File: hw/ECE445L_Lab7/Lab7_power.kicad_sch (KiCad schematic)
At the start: 0 parts

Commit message: Created spice models for analog circuits, started kicad schematic -> right audio channel, screen, basic power
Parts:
- added C11, C12: 4.7u, ECE445L:C_Axial_200mil, symbol ECE445L:C
- added C13: 0.1u, ECE445L:C_Axial_200mil, symbol ECE445L:C
- added IC1: LP2950-33LPRE3, ECE445L:TL431CLPM, symbol ECE445L:LP2950-33LPRE3
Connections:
- new net +3V3: C12.1, C13.1, IC1.1 (OUTPUT)
- new net +VBat: C11.1, IC1.3 (INPUT)
- new net GND: C11.2, C12.2, C13.2, IC1.2 (GND)
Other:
- note added: "+3V3 Regulator"

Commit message: Updated hardware schematic
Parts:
- added IC3: LM4041CILPR, ECE445L:ti_LM4041CILPR, symbol ti_LM4041CILPR:LM4041CILPR
- added R3: 1k, symbol Device:R
- added R4: 47k, symbol Device:R
- added R5: 10k, symbol Device:R
- renumbered IC1 to U2
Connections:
- net +3V3: now also R3.1
- net GND: now also IC3.3, R5.2
- new net: IC3.2, R3.2, R4.1
- new net VRef: IC3.1, R4.2, R5.1
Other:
- note added: "Vref"

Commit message: More Updates to hardware
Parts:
- added J3: Barrel_Jack, symbol Connector:Barrel_Jack
- renumbered U2 to U4, IC3 to U7
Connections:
- net +VBat: now also J3.1
- net GND: now also J3.2
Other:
- note added: "Wallwort Connector"
- moved on the sheet: R3, R4, R5, U7

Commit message: Lab7A Schematic and BOM - Ashton
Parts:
- removed U4: LP2950-33LPRE3, ECE445L:TL431CLPM, symbol ECE445L:LP2950-33LPRE3
- added SW8: SW_SPST, symbol Switch:SW_SPST
- added TP1: +VRail, ECE445L:Testpoint_1x02_P2.54mm, symbol ECE445L:Testpoint
- added TP13: +VRef, ECE445L:Testpoint_1x02_P2.54mm, symbol ECE445L:Testpoint
- added TP2: 3V3, ECE445L:Testpoint_1x02_P2.54mm, symbol ECE445L:Testpoint
- added U4: LM2937ET-3.3_NOPB, ECE445L:TO254P470X1028X1955-3P, symbol ECE445L:LM2937ET-3.3_NOPB
- C12: renamed from C11; footprint ECE445L:C_Axial_200mil -> Capacitor_SMD:C_0805_2012Metric
- C13: renamed from C12; footprint ECE445L:C_Axial_200mil -> Capacitor_SMD:C_0805_2012Metric
- C14: renamed from C13; footprint ECE445L:C_Axial_200mil -> Capacitor_SMD:C_0603_1608Metric
- renumbered R3 to R60, R4 to R61, R5 to R62
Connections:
- net +3V3: now also TP2.1 (A), TP2.2 (B), U4.3 (OUTPUT)
- net GND: now also U4.2 (GND)
- net VRef: now also TP13.1 (A), TP13.2 (B)
- net +VBat: no longer names the net of J3.1
- net +VBat: now also SW8.1 (A); no longer C12.1
- new net +VRail: C12.1, SW8.2 (B), TP1.1 (A), TP1.2 (B), U4.1 (INPUT)

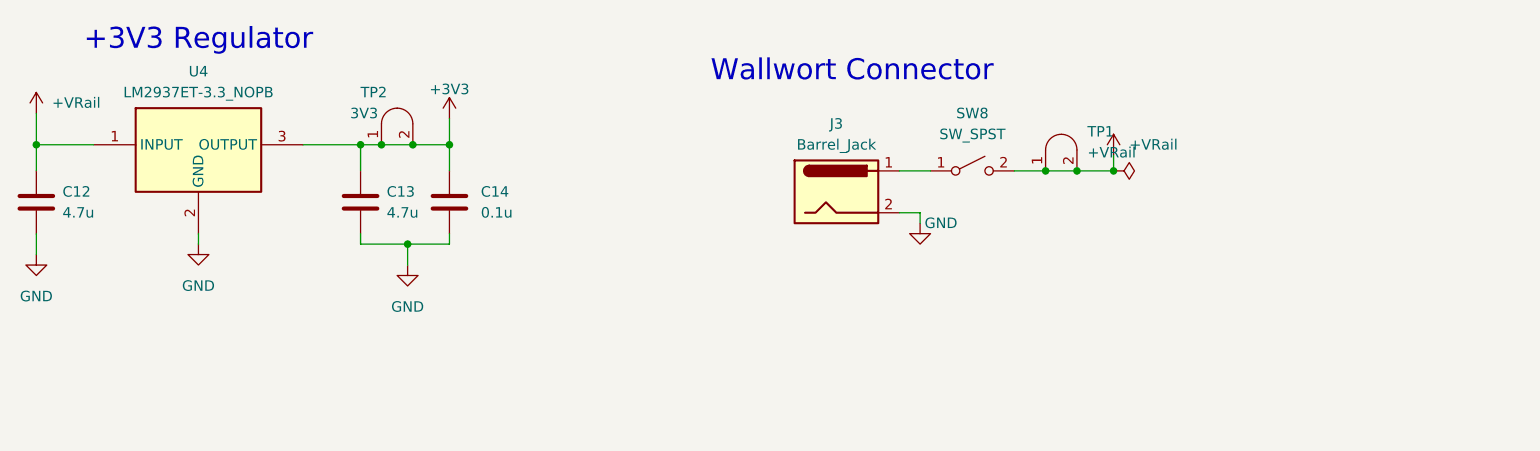
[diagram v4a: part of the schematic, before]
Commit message: Made changers to the schematic, updated bom, and created priliminary layout for the PCB. Ready for 7B Prep!
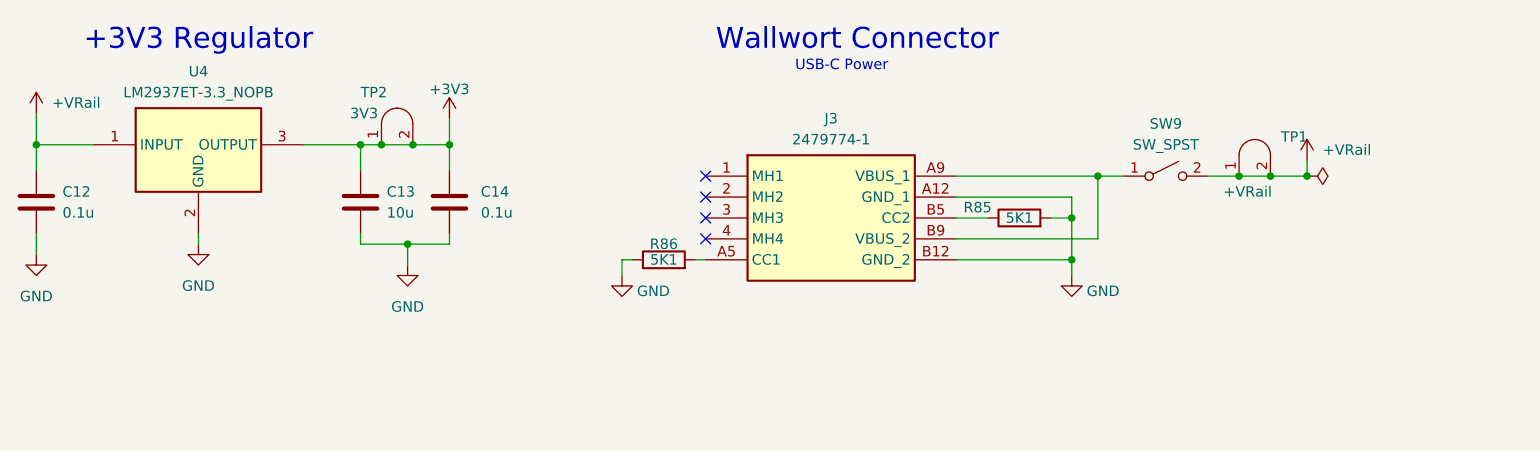
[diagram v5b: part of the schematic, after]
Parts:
- removed J3: Barrel_Jack, symbol Connector:Barrel_Jack
- added J3: 2479774-1, ECE445L:24797741, symbol 2479774-1:2479774-1
- added R85, R86: 5K1, Resistor_SMD:R_0603_1608Metric, symbol Device:R
- C12: value 4.7u -> 0.1u; footprint Capacitor_SMD:C_0805_2012Metric -> Capacitor_SMD:C_0603_1608Metric
- C13: value 4.7u -> 10u
- R60, R61, R62: footprint (none) -> Resistor_SMD:R_0603_1608Metric
- SW9: renamed from SW8; footprint (none) -> ECE445L:SW-T3-1A-A-A3-S1
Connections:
- net GND: now also J3.A12 (GND_1), J3.B12 (GND_2), R85.2, R86.1
- net at SW9.1 (A): now also J3.A9 (VBUS_1), J3.B9 (VBUS_2)
- new net: J3.B5 (CC2), R85.1
- new net: J3.A5 (CC1), R86.2
- no-connect marks 0 -> 4
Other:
- note added: "USB-C Power"
- moved on the sheet: SW9, TP1

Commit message: Rough draft layout - need to remove tm4c chip
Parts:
- C1: renamed from C12; footprint Capacitor_SMD:C_0603_1608Metric -> Capacitor_SMD:C_0603_1608Metric_Pad1.08x0.95mm_HandSolder
- C2: renamed from C13; footprint Capacitor_SMD:C_0805_2012Metric -> Capacitor_SMD:C_0805_2012Metric_Pad1.18x1.45mm_HandSolder
- C3: renamed from C14; footprint Capacitor_SMD:C_0603_1608Metric -> Capacitor_SMD:C_0603_1608Metric_Pad1.08x0.95mm_HandSolder
- R1: renamed from R86; footprint Resistor_SMD:R_0603_1608Metric -> Resistor_SMD:R_0603_1608Metric_Pad0.98x0.95mm_HandSolder
- R2: renamed from R85; footprint Resistor_SMD:R_0603_1608Metric -> Resistor_SMD:R_0603_1608Metric_Pad0.98x0.95mm_HandSolder
- R3: renamed from R60; footprint Resistor_SMD:R_0603_1608Metric -> Resistor_SMD:R_0603_1608Metric_Pad0.98x0.95mm_HandSolder
- R4: renamed from R61; footprint Resistor_SMD:R_0603_1608Metric -> Resistor_SMD:R_0603_1608Metric_Pad0.98x0.95mm_HandSolder
- R5: renamed from R62; footprint Resistor_SMD:R_0603_1608Metric -> Resistor_SMD:R_0603_1608Metric_Pad0.98x0.95mm_HandSolder
- renumbered J3 to J1, SW9 to SW1, TP2 to TP1, TP1 to TP2, TP13 to TP3, U4 to U1, U7 to U2
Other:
- company: (none) -> The University of Texas at Austin
- title: (none) -> ECE 445L Lab7

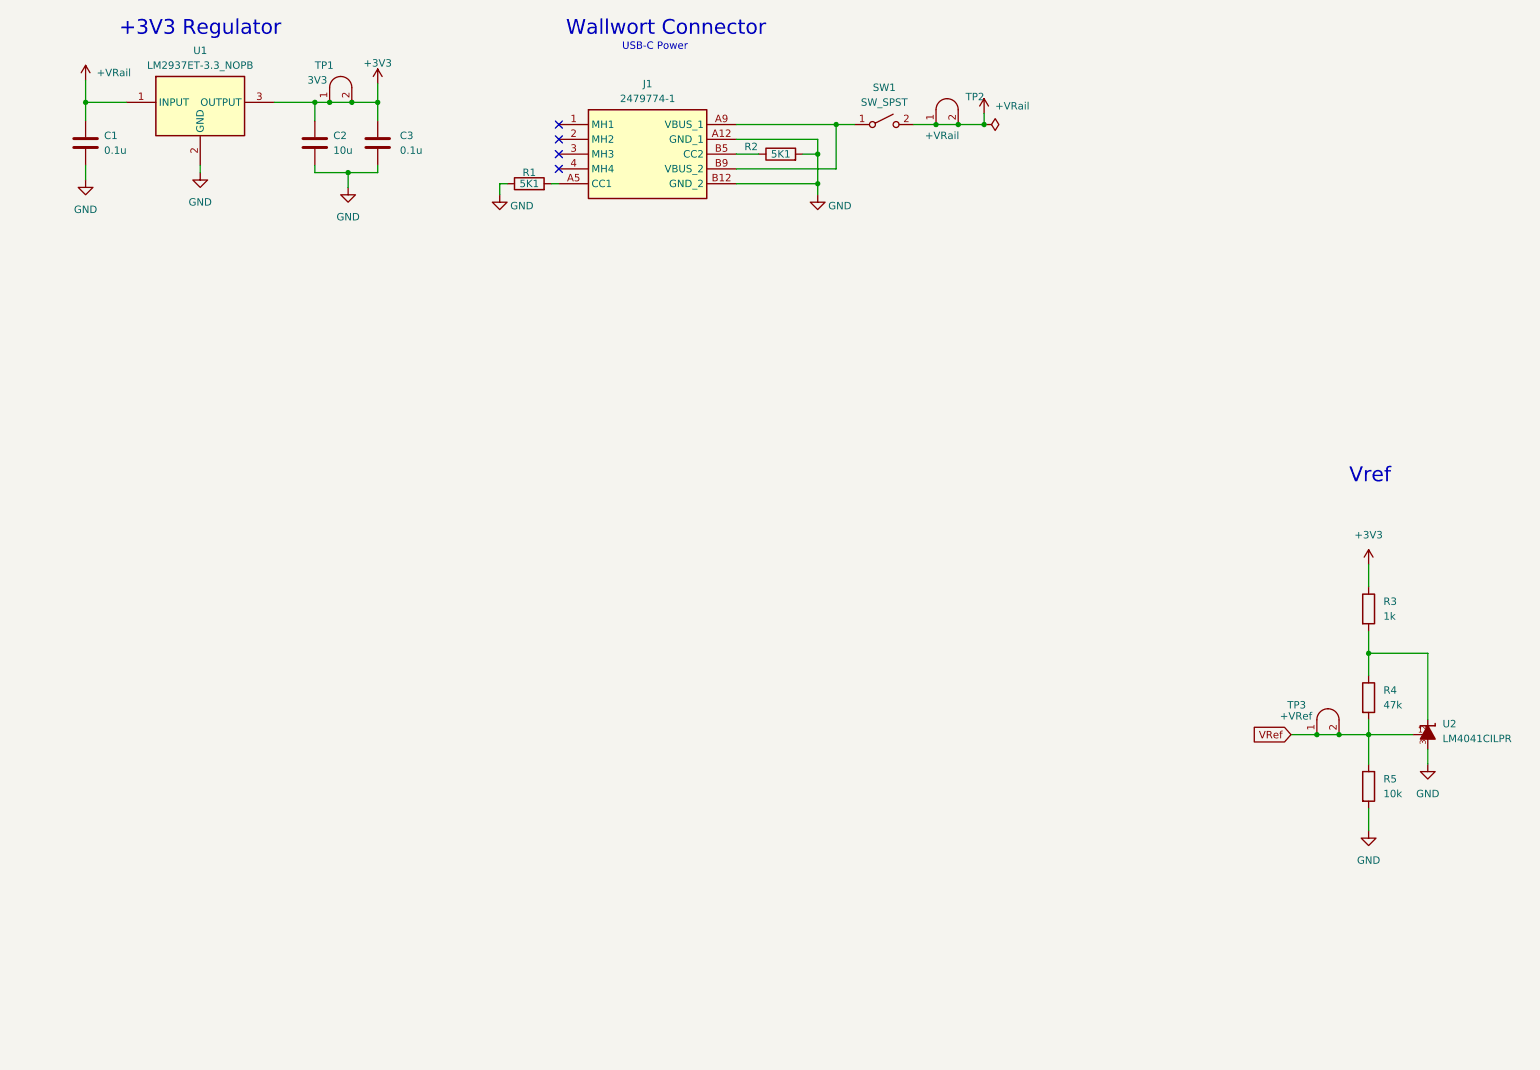
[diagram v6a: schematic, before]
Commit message: Added current consumption to schematic
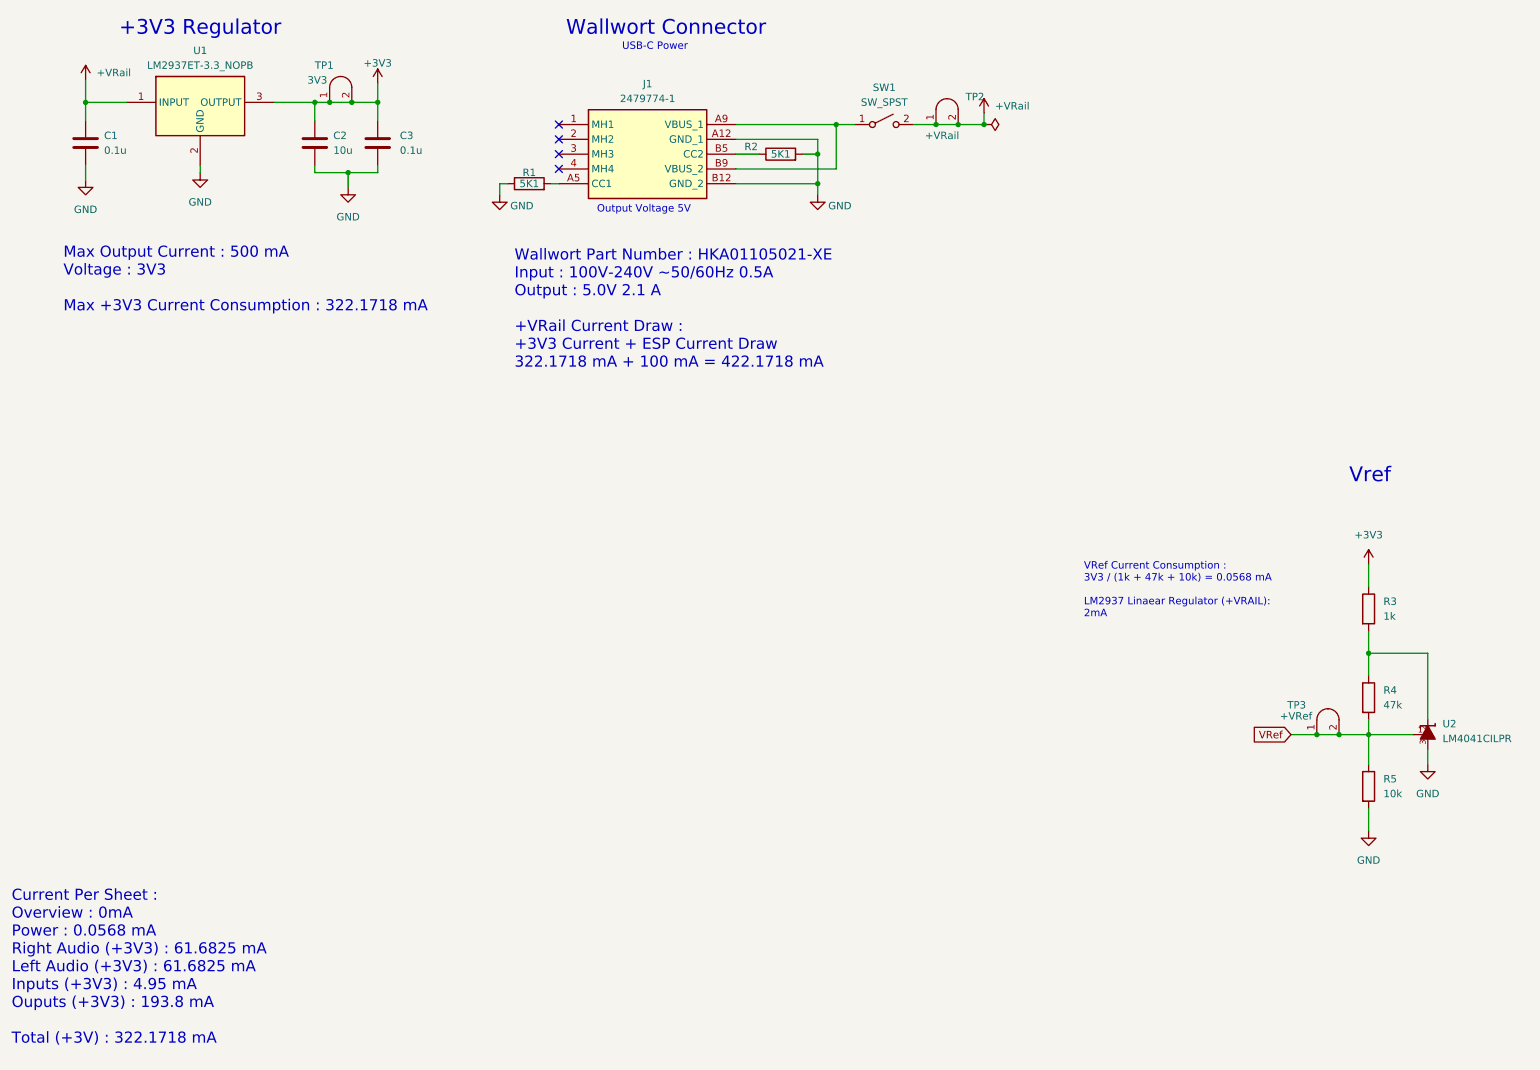
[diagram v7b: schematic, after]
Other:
- note added: "Current Per Sheet : Overview : 0mA Power : 0.0568 mA Right Audio (+3V3) : 61.6825 mA Left Audio (+3V3) : 61.6825 mA Inputs (+3V3) : 4.95 mA Ouputs (+3V3) : 193.8 mA Total (+3V) : 322.1718 mA"
- note added: "Max Output Current : 500 mA Voltage : 3V3 Max +3V3 Current Consumption : 322.1718 mA"
- note added: "Output Voltage 5V"
- note added: "VRef Current Consumption : 3V3 / (1k + 47k + 10k) = 0.0568 mA LM2937 Linaear Regulator (+VRAIL): 2mA"
- note added: "Wallwort Part Number : HKA01105021-XE Input : 100V-240V ~50/60Hz 0.5A Output : 5.0V 2.1 A +VRail Current Draw : +3V3 Current + ESP Current Draw 322.1718 mA + 100 mA = 422.1718 mA"
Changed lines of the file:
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@@
 		(comment 1 "Drawn By Ashton Knecht - atk836")
+	)
+	(text "Max Output Current : 500 mA\nVoltage : 3V3\n\nMax +3V3 Current Consumption : 322.1718 mA"
+		(exclude_from_sim no)
+		(at 24.765 62.23 0)
+		(effects
+			(font
+				(size 1.905 1.905)
+			)
+			(justify left)
+		)
+	)
+	(text "Wallwort Part Number : HKA01105021-XE\nInput : 100V-240V ~50/60Hz 0.5A\nOutput : 5.0V 2.1 A\n\n+VRail Current Draw :\n+3V3 Current + ESP Current Draw\n322.1718 mA + 100 mA = 422.1718 mA"
+		(exclude_from_sim no)
+		(at 102.235 67.31 0)
+		(effects
+			(font
+				(size 1.905 1.905)
+			)
+			(justify left)
+		)
+	)
+	(text "VRef Current Consumption :\n3V3 / (1k + 47k + 10k) = 0.0568 mA\n\nLM2937 Linaear Regulator (+VRAIL):\n2mA\n"
+		(exclude_from_sim no)
+		(at 200.025 115.57 0)
+		(effects
+			(font
+				(size 1.27 1.27)
+			)
+			(justify left)
+		)
 	)
 	(text "+3V3 Regulator"
@@
 			(font
 				(size 2.54 2.54)
+			)
+		)
+	)
+	(text "Output Voltage 5V\n"
+		(exclude_from_sim no)
+		(at 124.46 50.165 0)
+		(effects
+			(font
+				(size 1.27 1.27)
 			)
 		)
@@
 		)
 	)
+	(text "Current Per Sheet :\nOverview : 0mA\nPower : 0.0568 mA\nRight Audio (+3V3) : 61.6825 mA\nLeft Audio (+3V3) : 61.6825 mA\nInputs (+3V3) : 4.95 mA\nOuputs (+3V3) : 193.8 mA \n\nTotal (+3V) : 322.1718 mA\n"
+		(exclude_from_sim no)
+		(at 15.875 180.34 0)
+		(effects
+			(font
+				(size 1.905 1.905)
+			)
+			(justify left)
+		)
+	)

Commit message: Updated lab7a report
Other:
- note added: "+5V Laptop Current Consumption (Only FT2322R) : 15 mA"
- note added: "Current Per Sheet : Overview : 0mA Power : 0.0568 mA Microcontroller : 30 mA Right Audio (+3V3) : 61.6825 mA Left Audio (+3V3) : 61.6825 mA Inputs (+3V3) : 4.95 mA Ouputs (+3V3) : 193.8 mA Total (+3V) : 352.1718 mA"
- note added: "Power Sheet Current Consumption VRef Current Consumption : 3V3 / (1k + 47k + 10k) = 0.0568 mA LM2937 Linaear Regulator (+VRAIL): 2mA"
- note added: "Total Current Consumption for each Voltage : +3V3 : 352.1718 mA +VRAIL (+5V) : 452.1718 mA +5V Laptop : 15 mA"
- note added: "Wallwort Part Number : HKA01105021-XE Input : 100V-240V ~50/60Hz 0.5A Output : 5.0V 2.1 A +VRail Current Draw : +3V3 Current + ESP Current Draw 352.1718 mA + 100 mA = 452.1718 mA"
- note removed: "Current Per Sheet : Overview : 0mA Power : 0.0568 mA Right Audio (+3V3) : 61.6825 mA Left Audio (+3V3) : 61.6825 mA Inputs (+3V3) : 4.95 mA Ouputs (+3V3) : 193.8 mA Total (+3V) : 322.1718 mA"
- note removed: "VRef Current Consumption : 3V3 / (1k + 47k + 10k) = 0.0568 mA LM2937 Linaear Regulator (+VRAIL): 2mA"
- note removed: "Wallwort Part Number : HKA01105021-XE Input : 100V-240V ~50/60Hz 0.5A Output : 5.0V 2.1 A +VRail Current Draw : +3V3 Current + ESP Current Draw 322.1718 mA + 100 mA = 422.1718 mA"
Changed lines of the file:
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@@
 		)
 	)
-	(text "Wallwort Part Number : HKA01105021-XE\nInput : 100V-240V ~50/60Hz 0.5A\nOutput : 5.0V 2.1 A\n\n+VRail Current Draw :\n+3V3 Current + ESP Current Draw\n322.1718 mA + 100 mA = 422.1718 mA"
+	(text "Wallwort Part Number : HKA01105021-XE\nInput : 100V-240V ~50/60Hz 0.5A\nOutput : 5.0V 2.1 A\n\n+VRail Current Draw :\n+3V3 Current + ESP Current Draw\n352.1718 mA + 100 mA = 452.1718 mA"
 		(exclude_from_sim no)
 		(at 102.235 67.31 0)
@@
 		)
 	)
-	(text "VRef Current Consumption :\n3V3 / (1k + 47k + 10k) = 0.0568 mA\n\nLM2937 Linaear Regulator (+VRAIL):\n2mA\n"
+	(text "Power Sheet Current Consumption\n\nVRef Current Consumption :\n3V3 / (1k + 47k + 10k) = 0.0568 mA\n\nLM2937 Linaear Regulator (+VRAIL):\n2mA\n"
 		(exclude_from_sim no)
 		(at 200.025 115.57 0)
@@
 		)
 	)
+	(text "+5V Laptop Current Consumption (Only FT2322R) :\n15 mA"
+		(exclude_from_sim no)
+		(at 97.79 82.55 0)
+		(effects
+			(font
+				(size 1.905 1.905)
+			)
+			(justify left)
+		)
+	)
 	(text "USB-C Power"
 		(exclude_from_sim no)
@@
 		)
 	)
-	(text "Current Per Sheet :\nOverview : 0mA\nPower : 0.0568 mA\nRight Audio (+3V3) : 61.6825 mA\nLeft Audio (+3V3) : 61.6825 mA\nInputs (+3V3) : 4.95 mA\nOuputs (+3V3) : 193.8 mA \n\nTotal (+3V) : 322.1718 mA\n"
+	(text "Current Per Sheet :\nOverview : 0mA\nPower : 0.0568 mA\nMicrocontroller : 30 mA \nRight Audio (+3V3) : 61.6825 mA\nLeft Audio (+3V3) : 61.6825 mA\nInputs (+3V3) : 4.95 mA\nOuputs (+3V3) : 193.8 mA \n\nTotal (+3V) : 352.1718 mA\n"
 		(exclude_from_sim no)
 		(at 15.875 180.34 0)
@@
 		)
 	)
+	(text "Total Current Consumption for each Voltage :\n+3V3 : 352.1718 mA\n+VRAIL (+5V) : 452.1718 mA\n+5V Laptop : 15 mA"
+		(exclude_from_sim no)
+		(at 127.635 175.895 0)
+		(effects
+			(font
+				(size 2.54 2.54)
+			)
+		)
+	)
